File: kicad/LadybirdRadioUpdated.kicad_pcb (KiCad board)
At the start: 2 copper layers, 191.2 x 93.2 mm, 44 parts, among them J1 Conn_02x03_Odd_Even, J11 A/E, J12 VCap, J13 Conn_01x02_Pin, J14 Conn_01x02_Pin, J15 Conn_01x03_Pin, J16 Conn_01x02_Pin, J17 Conn_01x02_Pin, J18 Conn_01x02_Pin, J2 Conn_02x02_Odd_Even, J3 Conn_02x01, J4 Conn_02x03_Odd_Even, J5 Conn_02x03_Odd_Even, Q1 BC547, Q2 BC337, Q3 BC337, T1 P631T_LT700

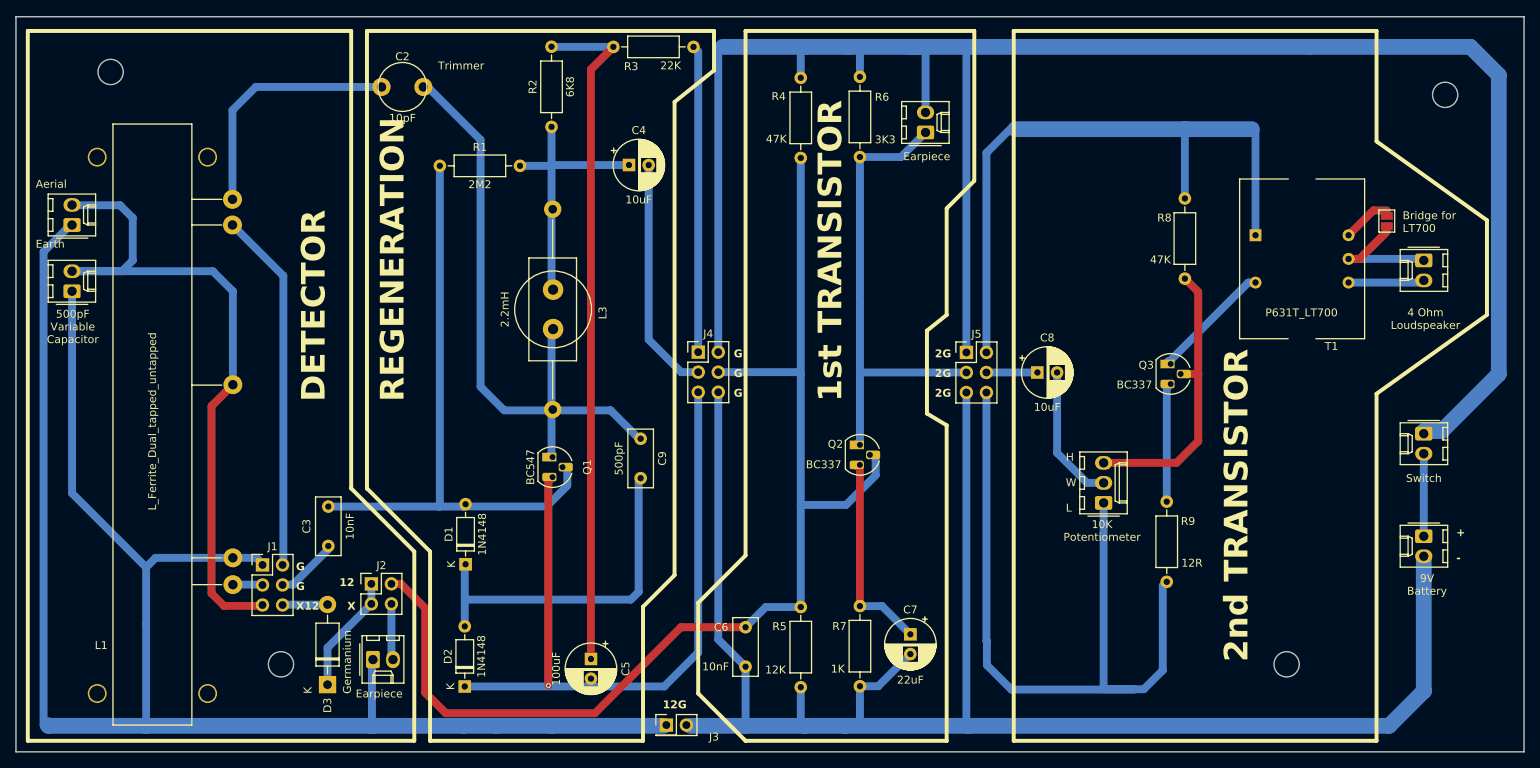
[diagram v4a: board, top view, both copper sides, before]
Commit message: Adjusted all labels to be the right way up and added Gerber files
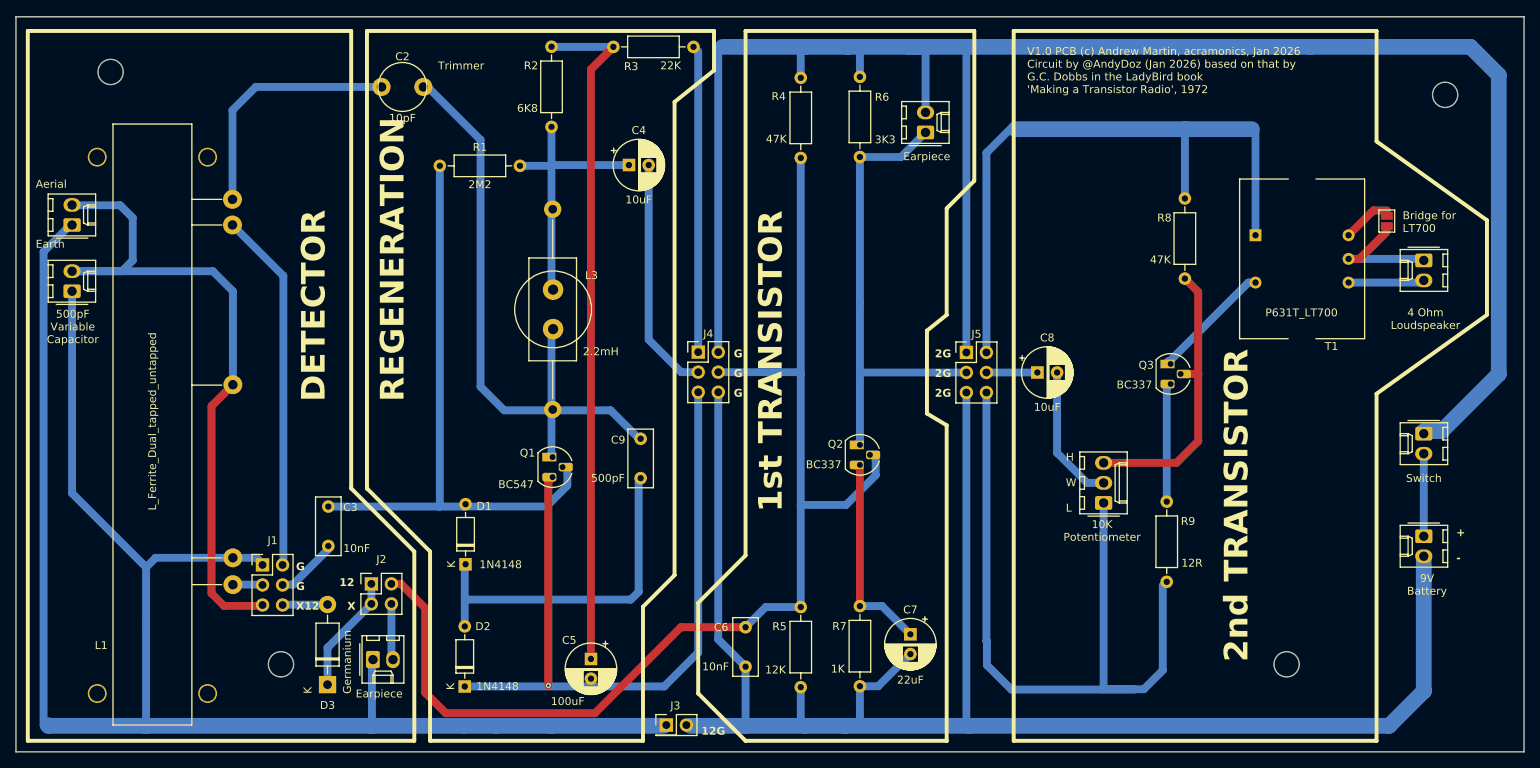
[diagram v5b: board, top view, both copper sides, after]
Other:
- board text added: "V1.0 PCB (c) Andrew Martin, acramonics, Jan 2026 Circuit by @AndyDoz (Jan 2026) based on that by G.C. Dobbs in the LadyBird book 'Making a Transistor Radio', 1972"
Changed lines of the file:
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@@
 			(outputformat 1)
 			(mirror no)
-			(drillshape 1)
+			(drillshape 0)
 			(scaleselection 1)
-			(outputdirectory "")
+			(outputdirectory "./gerber-LadyBird")
 		)
 	)
@@
 		(tags "CP Radial series Radial pin pitch 2.50mm  diameter 6.3mm Electrolytic Capacitor")
 		(property "Reference" "C5"
-			(at 1.25 -4.4 90)
+			(at -2.367621 2.75 0)
 			(layer "F.SilkS")
 			(effects
@@
 		)
 		(property "Value" "100uF"
-			(at 1.25 4.4 90)
+			(at 5.382379 2.95 0)
 			(layer "F.SilkS")
 			(effects
@@
 		(tags "Through hole pin header THT 2x02 2.54mm double row")
 		(property "Reference" "J2"
-			(at 1.27 -2.33 0)
+			(at 1.27 -3.1 0)
 			(layer "F.SilkS")
 			(effects
@@
 		(tags "Diode DO-35_SOD27 series Axial Horizontal pin pitch 7.62mm  length 4mm diameter 2mm")
 		(property "Reference" "D2"
-			(at 3.81 -2.12 90)
+			(at 7.61 2.3 0)
 			(layer "F.SilkS")
 			(effects
@@
 		)
 		(property "Value" "1N4148"
-			(at 3.81 2.12 90)
+			(at 0.01 4.15 0)
 			(layer "F.SilkS")
 			(effects
@@
 		(tags "C Rect series Radial pin pitch 5.00mm  length 7.2mm width 3.0mm Capacitor")
 		(property "Reference" "C3"
-			(at 2.5 -2.75 90)
+			(at 4.9 2.8 0)
 			(layer "F.SilkS")
 			(effects
@@
 		)
 		(property "Value" "10nF"
-			(at 2.5 2.75 90)
+			(at -0.3 3.6 0)
 			(layer "F.SilkS")
 			(effects
@@
 		(tags "Resistor Axial_DIN0207 series Axial Horizontal pin pitch 10.16mm 0.25W = 1/4W length 6.3mm diameter 2.5mm")
 		(property "Reference" "R2"
-			(at 5.08 -2.37 90)
+			(at 7.76 -2.6 0)
 			(layer "F.SilkS")
 			(effects
@@
 		)
 		(property "Value" "6K8"
-			(at 5.08 2.37 90)
+			(at 2.36 -3.05 0)
 			(layer "F.SilkS")
 			(effects
@@
 		(tags "C Rect series Radial pin pitch 5.00mm  length 7.2mm width 3.0mm Capacitor")
 		(property "Reference" "C9"
-			(at 2.5 -2.75 90)
+			(at 0.15 2.85 0)
 			(layer "F.SilkS")
 			(effects
@@
 		)
 		(property "Value" "500pF"
-			(at 2.5 2.75 90)
+			(at 5 4.15 0)
 			(layer "F.SilkS")
 			(effects
@@
 		(tags "to-92 sc-43 sc-43a sot54 PA33 transistor")
 		(property "Reference" "Q1"
-			(at 1.27 -4.4 90)
+			(at -0.53 3.18 0)
 			(layer "F.SilkS")
 			(effects
@@
 		)
 		(property "Value" "BC547"
-			(at 1.27 2.79 90)
+			(at 3.47 4.63 0)
 			(layer "F.SilkS")
 			(effects
@@
 		(tags "Diode DO-41_SOD81 series Axial Horizontal pin pitch 10.16mm  length 5.2mm diameter 2.7mm")
 		(property "Reference" "D3"
-			(at -2.62 0 90)
+			(at -2.62 0 0)
 			(layer "F.SilkS")
 			(effects
@@
 		(tags "Through hole pin header THT 2x03 2.54mm double row")
 		(property "Reference" "J1"
-			(at 1.27 -2.33 0)
+			(at 1.27 -3.1 0)
 			(layer "F.SilkS")
 			(effects
@@
 		(tags "Diode DO-35_SOD27 series Axial Horizontal pin pitch 7.62mm  length 4mm diameter 2mm")
 		(property "Reference" "D1"
-			(at 3.81 -2.12 90)
+			(at 7.37 2.35 0)
 			(layer "F.SilkS")
 			(effects
@@
 		)
 		(property "Value" "1N4148"
-			(at 3.81 2.12 90)
+			(at -0.03 4.45 0)
 			(layer "F.SilkS")
 			(effects
@@
 		(tags "Through hole pin header THT 2x01 2.54mm double row")
 		(property "Reference" "J3"
-			(at 6.04 1.5 0)
+			(at 1.14 -2.45 0)
 			(layer "F.SilkS")
 			(effects
@@
 		(tags "Inductor Axial series Axial Horizontal pin pitch 25.4mm  length 12.8mm diameter 5.8mm Fastron HBCC")
 		(property "Reference" "L3"
-			(at 13.15 -6.35 90)
+			(at 8.4 -4.92 0)
 			(layer "F.SilkS")
 			(effects
@@
 		)
 		(property "Value" "2.2mH"
-			(at 12.7 6.05 90)
+			(at 18.05 -6.1 0)
 			(layer "F.SilkS")
 			(effects
@@
 	)
 	(gr_text "12G"
-		(at 100.5 122 0)
+		(at 105.4 125.35 0)
 		(layer "F.SilkS")
 		(effects
@@
 	)
 	(gr_text "1st TRANSISTOR"
-		(at 123.5 83 90)
+		(at 115.95 97 90)
 		(layer "F.SilkS")
 		(effects
@@
 			)
 			(justify left bottom)
+		)
+	)
+	(gr_text "V1.0 PCB (c) Andrew Martin, acramonics, Jan 2026\nCircuit by @AndyDoz (Jan 2026) based on that by\nG.C. Dobbs in the LadyBird book\n'Making a Transistor Radio', 1972"
+		(at 146.7 44 0)
+		(layer "F.SilkS")
+		(effects
+			(font
+				(size 1 1)
+				(thickness 0.1)
+			)
+			(justify left bottom)

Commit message: Some final tweaks and first version ready
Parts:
- C9: value 500pF -> 470pF
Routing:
- net Net-(J15-Pin_1): track 98.3 -> 93.6 mm
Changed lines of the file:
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@@
 		(pad "" np_thru_hole circle
 			(at 4 -7 90)
-			(size 2.4 2.4)
-			(drill 2)
+			(size 2.9 2.9)
+			(drill 2.5)
 			(layers "*.Cu")
 		)
 		(pad "" np_thru_hole circle
 			(at 4 7 90)
-			(size 2.4 2.4)
-			(drill 2)
+			(size 2.9 2.9)
+			(drill 2.5)
 			(layers "*.Cu")
 		)
 		(pad "" np_thru_hole circle
 			(at 72 -7 90)
-			(size 2.4 2.4)
-			(drill 2)
+			(size 2.9 2.9)
+			(drill 2.5)
 			(layers "*.Cu")
 		)
 		(pad "" np_thru_hole circle
 			(at 72 7 90)
-			(size 2.4 2.4)
-			(drill 2)
+			(size 2.9 2.9)
+			(drill 2.5)
 			(layers "*.Cu")
 		)
@@
 			)
 		)
-		(property "Value" "500pF"
+		(property "Value" "470pF"
 			(at 5 4.15 0)
 			(layer "F.SilkS")
@@
 	)
 	(segment
-		(start 156.4 119.36)
-		(end 156.3 119.46)
+		(start 141.54 116.34)
+		(end 144.66 119.46)
 		(width 1)
 		(layer "B.Cu")
@@
 	)
 	(segment
-		(start 141.54 113.34)
-		(end 141.6 113.4)
+		(start 156.4 119.36)
+		(end 156.3 119.46)
 		(width 1)
 		(layer "B.Cu")
@@
 	)
 	(segment
-		(start 163.9 117.06)
-		(end 163.9 106.34)
-		(width 1)
-		(layer "B.Cu")
-		(net 23)
-	)
-	(segment
-		(start 161.5 119.46)
-		(end 163.9 117.06)
+		(start 160.26 119.46)
+		(end 164.45 115.27)
 		(width 1)
 		(layer "B.Cu")
@@
 	)
 	(segment
-		(start 141.6 116.4)
-		(end 144.7 119.5)
-		(width 1)
-		(layer "B.Cu")
-		(net 23)
-	)
-	(segment
-		(start 144.7 119.5)
-		(end 160.3 119.5)
-		(width 1)
-		(layer "B.Cu")
-		(net 23)
-	)
-	(segment
-		(start 141.6 113.4)
-		(end 141.6 116.4)
+		(start 141.54 81.84)
+		(end 141.54 116.34)
 		(width 1)
 		(layer "B.Cu")
@@
 	)
 	(segment
-		(start 156.3 119.46)
-		(end 161.5 119.46)
+		(start 144.66 119.46)
+		(end 160.26 119.46)
 		(width 1)
 		(layer "B.Cu")
@@
 	)
 	(segment
-		(start 141.54 81.84)
-		(end 141.54 113.34)
+		(start 164.45 115.27)
+		(end 164.45 105.89)
 		(width 1)
 		(layer "B.Cu")
@@
 	)
 	(segment
-		(start 163.9 106.34)
+		(start 164.45 105.89)
 		(end 164.4 105.84)
 		(width 1)
